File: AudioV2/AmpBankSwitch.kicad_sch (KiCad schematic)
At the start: 19 parts, among them U311 TMUX7612, U312 TMUX7612

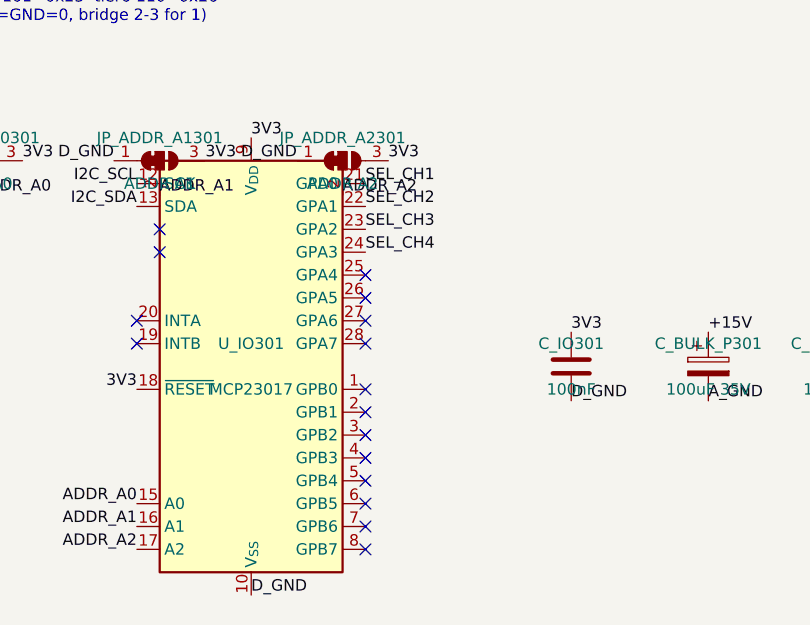
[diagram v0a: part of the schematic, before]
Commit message: AudioV2: AmpBankSwitch に MCP/ADDR を寄せ、親の SLOT SEL を外す
娘で SEL を出し、縦積み向け ADDR ジャンパと PCB デジタル島・AMP_SEL 取り回しを進める。

Co-authored-by: Cursor <cursoragent@cursor.com>
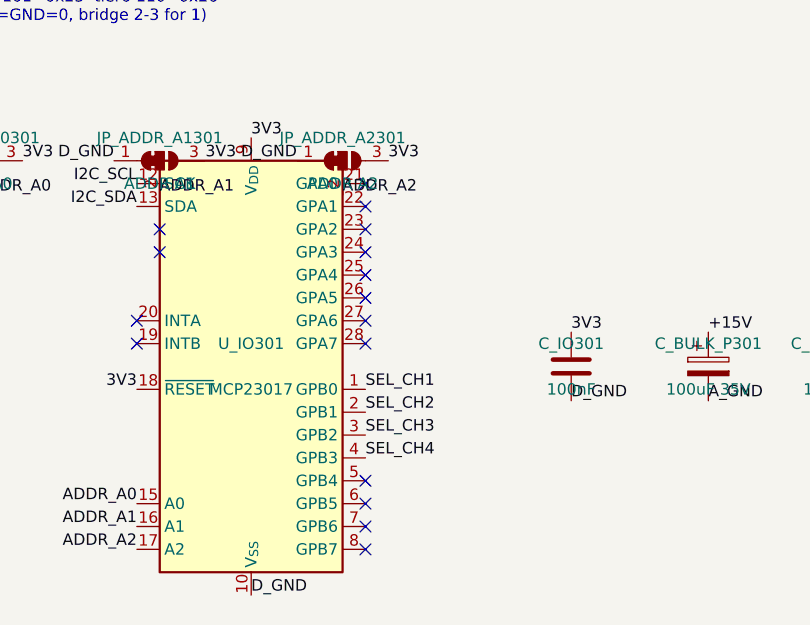
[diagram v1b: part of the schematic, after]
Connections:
- net SEL_CH1: now also U_IO301.1 (GPB0); no longer U_IO301.21 (GPA0)
- net SEL_CH2: now also U_IO301.2 (GPB1); no longer U_IO301.22 (GPA1)
- net SEL_CH3: now also U_IO301.3 (GPB2); no longer U_IO301.23 (GPA2)
- net SEL_CH4: now also U_IO301.4 (GPB3); no longer U_IO301.24 (GPA3)
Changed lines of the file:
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@@
 	)
 	(no_connect
-		(at 213.36 215.9)
+		(at 213.36 193.04)
 	)
 	(no_connect
@@
 	)
 	(no_connect
-		(at 213.36 218.44)
+		(at 213.36 195.58)
 	)
 	(no_connect
@@
 	)
 	(no_connect
-		(at 213.36 223.52)
+		(at 213.36 200.66)
 	)
 	(no_connect
@@
 	)
 	(no_connect
-		(at 213.36 220.98)
+		(at 213.36 198.12)
 	)
 	(no_connect
@@
 	)
 	(label "SEL_CH3"
-		(at 213.36 198.12 0)
+		(at 213.36 220.98 0)
 		(effects
 			(font
@@
 	)
 	(label "SEL_CH1"
-		(at 213.36 193.04 0)
+		(at 213.36 215.9 0)
 		(effects
 			(font
@@
 	)
 	(label "SEL_CH2"
-		(at 213.36 195.58 0)
+		(at 213.36 218.44 0)
 		(effects
 			(font
@@
 	)
 	(label "SEL_CH4"
-		(at 213.36 200.66 0)
-		(effects
-			(font
+		(at 213.36 223.52 0)
+		(effects
+			(font

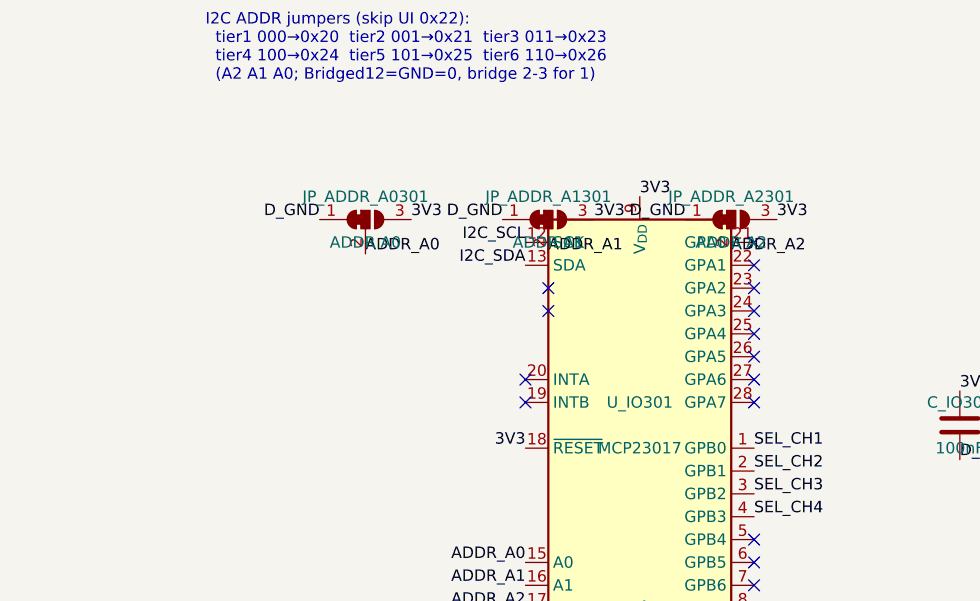
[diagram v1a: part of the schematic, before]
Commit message: AudioV2: ADDR ジャンパ参照を S_/R_ に揃え、早見表シルクを見やすく
Switch/Relay のジャンパを S_ADDR_* / R_ADDR_* に改名し、PCB シルクの番地表記を A2/A1/A0 形式に更新。

Co-authored-by: Cursor <cursoragent@cursor.com>
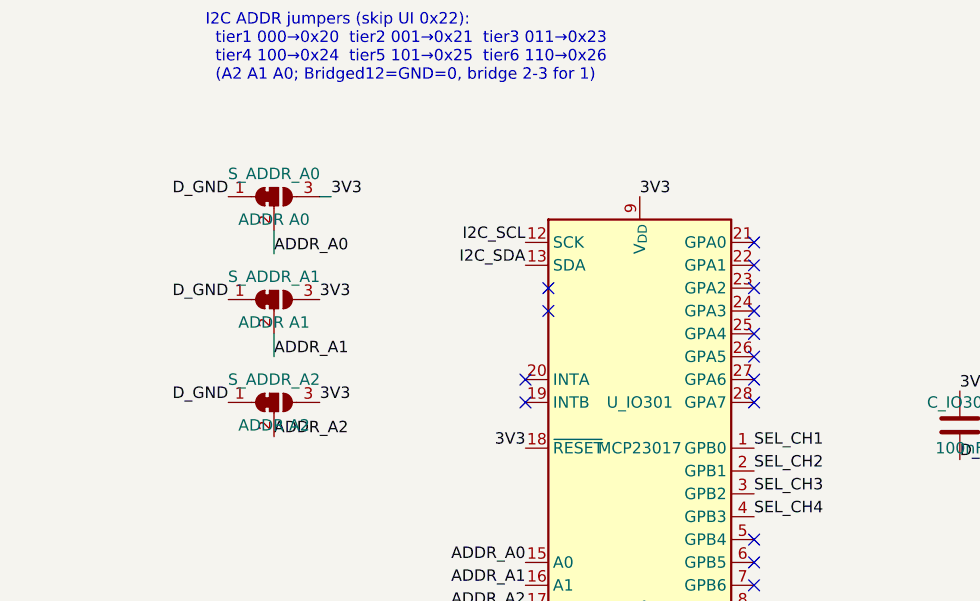
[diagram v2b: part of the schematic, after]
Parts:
- renumbered JP_ADDR_A0301 to S_ADDR_A0, JP_ADDR_A1301 to S_ADDR_A1, JP_ADDR_A2301 to S_ADDR_A2
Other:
- moved on the sheet: S_ADDR_A0, S_ADDR_A1, S_ADDR_A2
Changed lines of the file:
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@@
 		(at 213.36 205.74)
+	)
+	(wire
+		(pts
+			(xy 160.02 191.77) (xy 160.02 194.31)
+		)
+		(stroke
+			(width 0)
+			(type default)
+		)
+	)
+	(wire
+		(pts
+			(xy 165.1 187.96) (xy 166.37 187.96)
+		)
+		(stroke
+			(width 0)
+			(type default)
+		)
+	)
+	(wire
+		(pts
+			(xy 160.02 205.74) (xy 160.02 203.2)
+		)
+		(stroke
+			(width 0)
+			(type default)
+		)
 	)
 	(label "A_GND"
@@
 	)
 	(label "ADDR_A0"
-		(at 170.18 194.31 0)
+		(at 160.02 194.31 0)
 		(effects
 			(font
@@
 	)
 	(label "3V3"
-		(at 175.26 190.5 0)
+		(at 166.37 187.96 0)
 		(effects
 			(font
@@
 	)
 	(label "ADDR_A2"
-		(at 210.82 194.31 0)
+		(at 160.02 214.63 0)
 		(effects
 			(font
@@
 	)
 	(label "D_GND"
-		(at 165.1 190.5 180)
+		(at 154.94 187.96 180)
 		(effects
 			(font
@@
 	)
 	(label "D_GND"
-		(at 185.42 190.5 180)
+		(at 154.94 199.39 180)
 		(effects
 			(font
@@
 	)
 	(label "3V3"
-		(at 195.58 190.5 0)
+		(at 165.1 199.39 0)
 		(effects
 			(font
@@
 	)
 	(label "3V3"
-		(at 215.9 190.5 0)
+		(at 165.1 210.82 0)
 		(effects
 			(font
@@
 	)
 	(label "ADDR_A1"
-		(at 190.5 194.31 0)
+		(at 160.02 205.74 0)
 		(effects
 			(font
@@
 	)
 	(label "D_GND"
-		(at 205.74 190.5 180)
+		(at 154.94 210.82 180)
 		(effects
 			(font
@@
 	(symbol
 		(lib_id "Jumper:SolderJumper_3_Bridged12")
-		(at 210.82 190.5 0)
+		(at 160.02 210.82 0)
 		(unit 1)
 		(body_style 1)
@@
 		(dnp no)
 		(fields_autoplaced yes)
-		(property "Reference" "JP_ADDR_A2301"
-			(at 210.82 187.96 0)
+		(property "Reference" "S_ADDR_A2"
+			(at 160.02 208.28 0)
 			(show_name no)
 			(do_not_autoplace no)
@@
 		)
 		(property "Value" "ADDR A2"
-			(at 210.82 193.04 0)
+			(at 160.02 213.36 0)
 			(show_name no)
 			(do_not_autoplace no)
@@
 		)
 		(property "Footprint" "Jumper:SolderJumper-3_P1.3mm_Bridged12_Pad1.0x1.5mm_NumberLabels"
-			(at 0 0 0)
+			(at -50.8 20.32 0)
 			(hide yes)
 			(show_name no)
@@
 		)
 		(property "Datasheet" ""
-			(at 0 0 0)
+			(at -50.8 20.32 0)
 			(hide yes)
 			(show_name no)
@@
 		)
 		(property "Description" ""
-			(at 0 0 0)
+			(at -50.8 20.32 0)
 			(hide yes)
 			(show_name no)
@@
 			(project "AudioV2Case"
 				(path "/a1000001-0001-4001-8001-000000000001/a1000011-0011-4011-8011-000000000011"
-					(reference "JP_ADDR_A2301")
+					(reference "S_ADDR_A2")
 					(unit 1)
 				)
@@
 	(symbol
 		(lib_id "Jumper:SolderJumper_3_Bridged12")
-		(at 170.18 190.5 0)
+		(at 160.02 187.96 0)
 		(unit 1)
 		(body_style 1)
@@
 		(dnp no)
 		(fields_autoplaced yes)
-		(property "Reference" "JP_ADDR_A0301"
-			(at 170.18 187.96 0)
+		(property "Reference" "S_ADDR_A0"
+			(at 160.02 185.42 0)
 			(show_name no)
 			(do_not_autoplace no)
@@
 		)
 		(property "Value" "ADDR A0"
-			(at 170.18 193.04 0)
+			(at 160.02 190.5 0)
 			(show_name no)
 			(do_not_autoplace no)
@@
 		)
 		(property "Footprint" "Jumper:SolderJumper-3_P1.3mm_Bridged12_Pad1.0x1.5mm_NumberLabels"
-			(at 0 0 0)
+			(at -10.16 -2.54 0)
 			(hide yes)
 			(show_name no)
@@
 		)
 		(property "Datasheet" ""
-			(at 0 0 0)
+			(at -10.16 -2.54 0)
 			(hide yes)
 			(show_name no)
@@
 		)
 		(property "Description" ""
-			(at 0 0 0)
+			(at -10.16 -2.54 0)
 			(hide yes)
 			(show_name no)
@@
 			(project "AudioV2Case"
 				(path "/a1000001-0001-4001-8001-000000000001/a1000011-0011-4011-8011-000000000011"
-					(reference "JP_ADDR_A0301")
+					(reference "S_ADDR_A0")
 					(unit 1)
 				)
@@
 	(symbol
 		(lib_id "Jumper:SolderJumper_3_Bridged12")
-		(at 190.5 190.5 0)
+		(at 160.02 199.39 0)
 		(unit 1)
 		(body_style 1)
@@
 		(dnp no)
 		(fields_autoplaced yes)
-		(property "Reference" "JP_ADDR_A1301"
-			(at 190.5 187.96 0)
+		(property "Reference" "S_ADDR_A1"
+			(at 160.02 196.85 0)
 			(show_name no)
 			(do_not_autoplace no)
@@
 		)
 		(property "Value" "ADDR A1"
-			(at 190.5 193.04 0)
+			(at 160.02 201.93 0)
 			(show_name no)
 			(do_not_autoplace no)
@@
 		)
 		(property "Footprint" "Jumper:SolderJumper-3_P1.3mm_Bridged12_Pad1.0x1.5mm_NumberLabels"
-			(at 0 0 0)
+			(at -30.48 8.89 0)
 			(hide yes)
 			(show_name no)
@@
 		)
 		(property "Datasheet" ""
-			(at 0 0 0)
+			(at -30.48 8.89 0)
 			(hide yes)
 			(show_name no)
@@
 		)
 		(property "Description" ""
-			(at 0 0 0)
+			(at -30.48 8.89 0)
 			(hide yes)
 			(show_name no)
@@
 			(project "AudioV2Case"
 				(path "/a1000001-0001-4001-8001-000000000001/a1000011-0011-4011-8011-000000000011"
-					(reference "JP_ADDR_A1301")
+					(reference "S_ADDR_A1")
 					(unit 1)
 				)

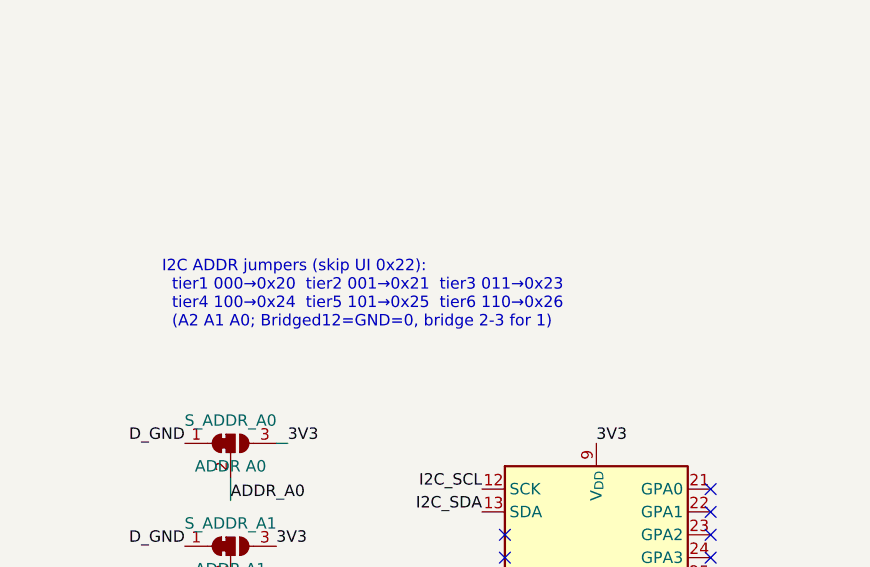
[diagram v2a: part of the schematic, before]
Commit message: AudioV2: ADDR 参照・注記を build_daughter に書き戻す
Relay ジャンパを R_ADDR_A* にし、番地早見の文言を sch/PCB と揃えた。再生成はしていない。

Co-authored-by: Cursor <cursoragent@cursor.com>
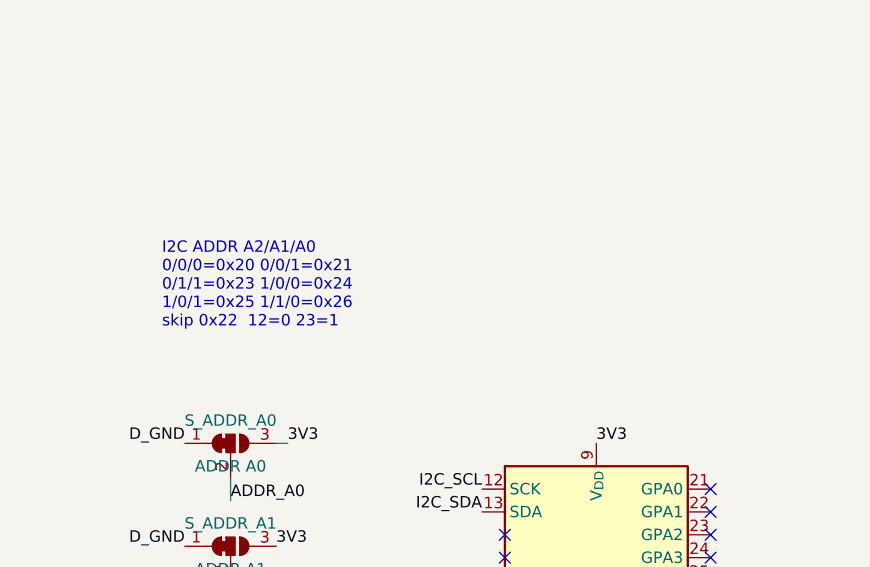
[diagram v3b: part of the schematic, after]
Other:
- note added: "I2C ADDR A2/A1/A0 0/0/0=0x20 0/0/1=0x21 0/1/1=0x23 1/0/0=0x24 1/0/1=0x25 1/1/0=0x26 skip 0x22 12=0 23=1"
- note removed: "I2C ADDR jumpers (skip UI 0x22): tier1 000→0x20 tier2 001→0x21 tier3 011→0x23 tier4 100→0x24 tier5 101→0x25 tier6 110→0x26 (A2 A1 A0; Bridged12=GND=0, bridge 2-3 for 1)"
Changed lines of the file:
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@@
 	(generator_version "10.0")
 	(paper "A2")
-	(text "I2C ADDR jumpers (skip UI 0x22):\n  tier1 000→0x20  tier2 001→0x21  tier3 011→0x23\n  tier4 100→0x24  tier5 101→0x25  tier6 110→0x26\n  (A2 A1 A0; Bridged12=GND=0, bridge 2-3 for 1)"
+	(text "I2C ADDR A2/A1/A0
+0/0/0=0x20 0/0/1=0x21
+0/1/1=0x23 1/0/0=0x24
+1/0/1=0x25 1/1/0=0x26
+skip 0x22  12=0 23=1"
 		(exclude_from_sim no)
 		(at 152.4 175.26 0)
